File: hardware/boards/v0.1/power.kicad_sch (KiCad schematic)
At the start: 31 parts, among them IC3 SP3401-02UTG, J2 USB, U20 TPS62A02DRL, U23 BQ21040DBV, U31 FUSB302B01MPX, U32 LTC2942

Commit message: feat: route audio components
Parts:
- C17, C18, R29: footprint Capacitor_SMD:C_0402_1005Metric -> Capacitor_SMD:C_0603_1608Metric
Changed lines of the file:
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@@
 			)
 		)
-		(property "Footprint" "Capacitor_SMD:C_0402_1005Metric"
+		(property "Footprint" "Capacitor_SMD:C_0603_1608Metric"
 			(at 104.14 30.48 0)
 			(effects
@@
 			)
 		)
-		(property "Footprint" "Capacitor_SMD:C_0402_1005Metric"
+		(property "Footprint" "Capacitor_SMD:C_0603_1608Metric"
 			(at 127.508 46.99 90)
 			(effects
@@
 			)
 		)
-		(property "Footprint" "Capacitor_SMD:C_0402_1005Metric"
+		(property "Footprint" "Capacitor_SMD:C_0603_1608Metric"
 			(at 96.52 30.48 0)
 			(effects

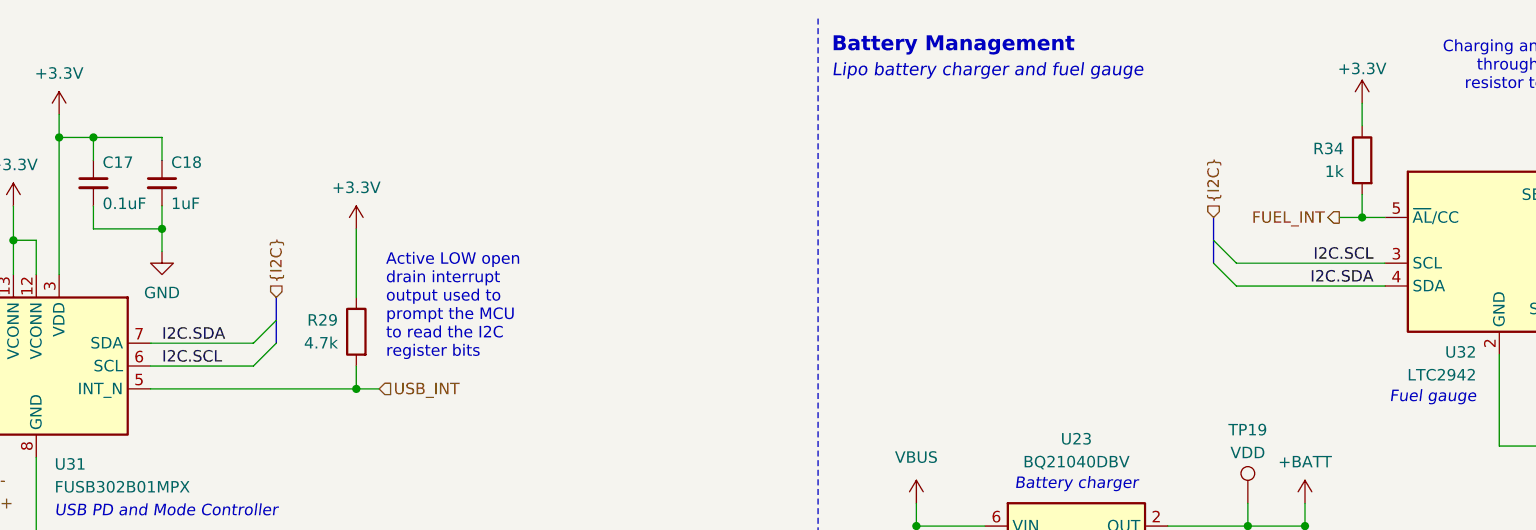
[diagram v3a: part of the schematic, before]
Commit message: feat: route dedicated audio I2C bus
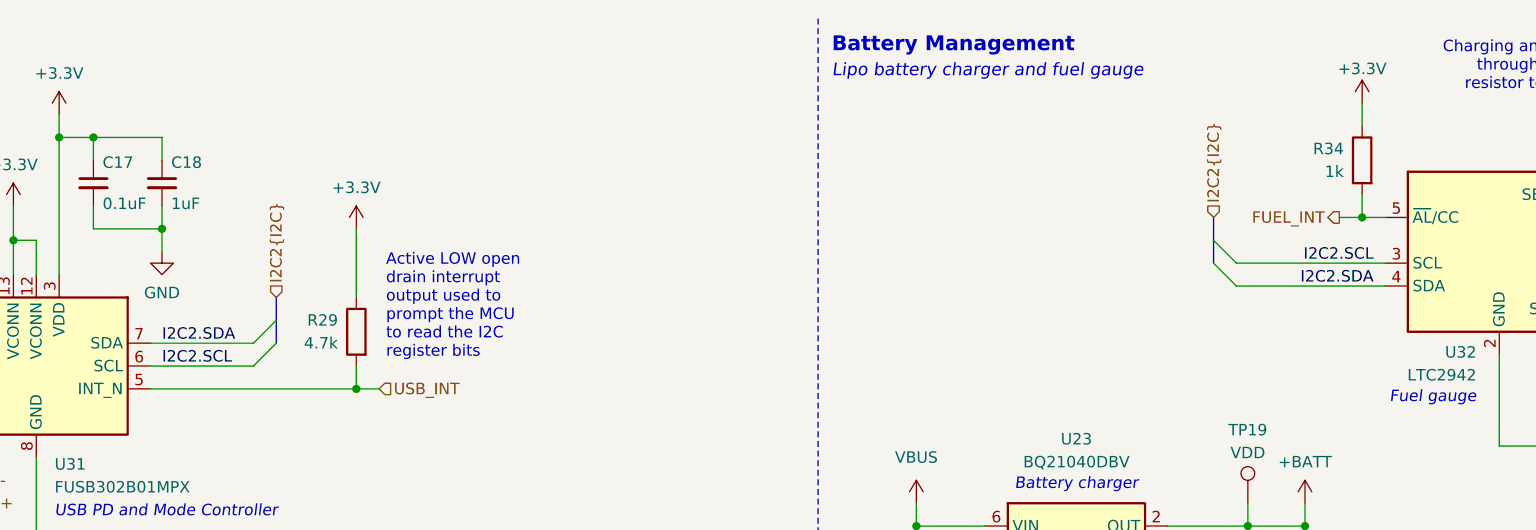
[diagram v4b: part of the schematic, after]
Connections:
- net I2C.SCL renamed I2C2.SCL
- net I2C.SDA renamed I2C2.SDA
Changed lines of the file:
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@@
 		)
 	)
-	(label "I2C.SCL"
+	(label "I2C2.SCL"
 		(at 238.76 39.37 180)
 		(effects
@@
 		)
 	)
-	(label "I2C.SDA"
+	(label "I2C2.SDA"
 		(at 104.14 48.26 0)
 		(effects
@@
 		)
 	)
-	(label "I2C.SDA"
+	(label "I2C2.SDA"
 		(at 238.76 41.91 180)
 		(effects
@@
 		)
 	)
-	(label "I2C.SCL"
+	(label "I2C2.SCL"
 		(at 104.14 50.8 0)
 		(effects
@@
 		)
 	)
-	(hierarchical_label "{I2C}"
+	(hierarchical_label "I2C2{I2C}"
 		(shape input)
 		(at 116.84 43.18 90)
@@
 		)
 	)
-	(hierarchical_label "{I2C}"
+	(hierarchical_label "I2C2{I2C}"
 		(shape input)
 		(at 220.98 34.29 90)

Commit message: feat: power system routing
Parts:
- added TP20: GND, TestPoint:TestPoint_Pad_D1.0mm, symbol Connector:TestPoint
- C12, C13, C9: footprint Capacitor_SMD:C_0805_2012Metric -> Capacitor_SMD:C_0603_1608Metric
- R2, R63, R72: footprint Capacitor_SMD:C_0402_1005Metric -> Resistor_SMD:R_0603_1608Metric
- R29: footprint Capacitor_SMD:C_0603_1608Metric -> Resistor_SMD:R_0603_1608Metric
- R33: value 100m -> 12m; footprint Capacitor_SMD:C_0402_1005Metric -> Resistor_SMD:R_2512_6332Metric_Pad1.40x3.35mm_HandSolder
- R34, R38: footprint Resistor_SMD:R_0402_1005Metric -> Resistor_SMD:R_0603_1608Metric
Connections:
- net GND: now also TP20.1
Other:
- note added: "I2C Address 1100100"
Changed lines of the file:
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@@
 		)
 	)
+	(text "I2C Address\n1100100"
+		(exclude_from_sim no)
+		(at 239.776 45.974 0)
+		(effects
+			(font
+				(size 1.27 1.27)
+				(color 132 132 132 1)
+			)
+			(justify right)
+		)
+	)
 	(text "Used by the STM32 to detect when a USB\ncable has been plugged in or removed.\n\nExpected signal < 4v"
 		(exclude_from_sim no)
@@
 	)
 	(junction
+		(at 212.09 86.36)
+		(diameter 0)
+		(color 0 0 0 0)
+	)
+	(junction
 		(at 67.31 153.67)
 		(diameter 0)
@@
 	(wire
 		(pts
-			(xy 205.74 86.36) (xy 223.52 86.36)
+			(xy 205.74 86.36) (xy 212.09 86.36)
 		)
 		(stroke
@@
 	(wire
 		(pts
+			(xy 212.09 86.36) (xy 223.52 86.36)
+		)
+		(stroke
+			(width 0)
+			(type default)
+		)
+	)
+	(wire
+		(pts
 			(xy 49.53 156.21) (xy 44.45 156.21)
 		)
@@
 	(wire
 		(pts
+			(xy 212.09 86.36) (xy 212.09 88.9)
+		)
+		(stroke
+			(width 0)
+			(type default)
+		)
+	)
+	(wire
+		(pts
 			(xy 72.39 185.42) (xy 72.39 186.69)
 		)
@@
 			)
 		)
-		(property "Value" "100m"
+		(property "Value" "12m"
 			(at 272.288 39.37 0)
 			(effects
@@
 			)
 		)
-		(property "Footprint" "Capacitor_SMD:C_0402_1005Metric"
+		(property "Footprint" "Resistor_SMD:R_2512_6332Metric_Pad1.40x3.35mm_HandSolder"
 			(at 276.098 38.1 90)
 			(effects
@@
 	)
 	(symbol
+		(lib_id "Connector:TestPoint")
+		(at 212.09 88.9 180)
+		(unit 1)
+		(exclude_from_sim no)
+		(in_bom yes)
+		(on_board yes)
+		(dnp no)
+		(property "Reference" "TP20"
+			(at 212.09 97.028 0)
+			(effects
+				(font
+					(size 1.27 1.27)
+				)
+			)
+		)
+		(property "Value" "GND"
+			(at 212.09 94.488 0)
+			(effects
+				(font
+					(size 1.27 1.27)
+				)
+			)
+		)
+		(property "Footprint" "TestPoint:TestPoint_Pad_D1.0mm"
+			(at 207.01 88.9 0)
+			(effects
+				(font
+					(size 1.27 1.27)
+				)
+				(hide yes)
+			)
+		)
+		(property "Datasheet" "~"
+			(at 207.01 88.9 0)
+			(effects
+				(font
+					(size 1.27 1.27)
+				)
+				(hide yes)
+			)
+		)
+		(property "Description" "test point"
+			(at 212.09 88.9 0)
+			(effects
+				(font
+					(size 1.27 1.27)
+				)
+				(hide yes)
+			)
+		)
+		(property "Arrow Part Number" ""
+			(at 212.09 88.9 0)
+			(effects
+				(font
+					(size 1.27 1.27)
+				)
+			)
+		)
+		(property "Arrow Price/Stock" ""
+			(at 212.09 88.9 0)
+			(effects
+				(font
+					(size 1.27 1.27)
+				)
+			)
+		)
+		(property "MANUFACTURER" ""
+			(at 212.09 88.9 0)
+			(effects
+				(font
+					(size 1.27 1.27)
+				)
+			)
+		)
+		(property "MAXIMUM_PACKAGE_HEIGHT" ""
+			(at 212.09 88.9 0)
+			(effects
+				(font
+					(size 1.27 1.27)
+				)
+			)
+		)
+		(property "PARTREV" ""
+			(at 212.09 88.9 0)
+			(effects
+				(font
+					(size 1.27 1.27)
+				)
+			)
+		)
+		(property "STANDARD" ""
+			(at 212.09 88.9 0)
+			(effects
+				(font
+					(size 1.27 1.27)
+				)
+			)
+		)
+		(property "Connector" ""
+			(at 212.09 88.9 0)
+			(effects
+				(font
+					(size 1.27 1.27)
+				)
+			)
+		)
+		(pin "1"
+		)
+		(instances
+			(project "pocket_synth"
+				(path "/485383b8-00f4-4405-b270-de249939cff4/4ddef61a-efa7-4012-86d6-37c4f1088d14"
+					(reference "TP20")
+					(unit 1)
+				)
+			)
+		)
+	)
+	(symbol
 		(lib_id "power:GND")
 		(at 205.74 88.9 0)
@@
 			)
 		)
-		(property "Footprint" "Resistor_SMD:R_0402_1005Metric"
+		(property "Footprint" "Resistor_SMD:R_0603_1608Metric"
 			(at 239.268 27.94 90)
 			(effects
@@
 			)
 		)
-		(property "Footprint" "Capacitor_SMD:C_0805_2012Metric"
+		(property "Footprint" "Capacitor_SMD:C_0603_1608Metric"
 			(at 75.2348 163.83 0)
 			(effects
@@
 			)
 		)
-		(property "Footprint" "Resistor_SMD:R_0402_1005Metric"
+		(property "Footprint" "Resistor_SMD:R_0603_1608Metric"
 			(at 191.262 80.01 90)
 			(effects
@@
 			)
 		)
-		(property "Footprint" "Capacitor_SMD:C_0402_1005Metric"
+		(property "Footprint" "Resistor_SMD:R_0603_1608Metric"
 			(at 72.39 189.23 0)
 			(effects
@@
 			)
 		)
-		(property "Footprint" "Capacitor_SMD:C_0805_2012Metric"
+		(property "Footprint" "Capacitor_SMD:C_0603_1608Metric"
 			(at 17.4752 175.26 0)
 			(effects
@@
 			)
 		)
-		(property "Footprint" "Capacitor_SMD:C_0402_1005Metric"
+		(property "Footprint" "Resistor_SMD:R_0603_1608Metric"
 			(at 91.948 179.07 90)
 			(effects
@@
 			)
 		)
-		(property "Footprint" "Capacitor_SMD:C_0603_1608Metric"
+		(property "Footprint" "Resistor_SMD:R_0603_1608Metric"
 			(at 127.508 46.99 90)
 			(effects
@@
 			)
 		)
-		(property "Footprint" "Capacitor_SMD:C_0805_2012Metric"
+		(property "Footprint" "Capacitor_SMD:C_0603_1608Metric"
 			(at 66.3448 163.83 0)
 			(effects
@@
 			)
 		)
-		(property "Footprint" "Capacitor_SMD:C_0402_1005Metric"
+		(property "Footprint" "Resistor_SMD:R_0603_1608Metric"
 			(at 77.47 194.31 0)
 			(effects

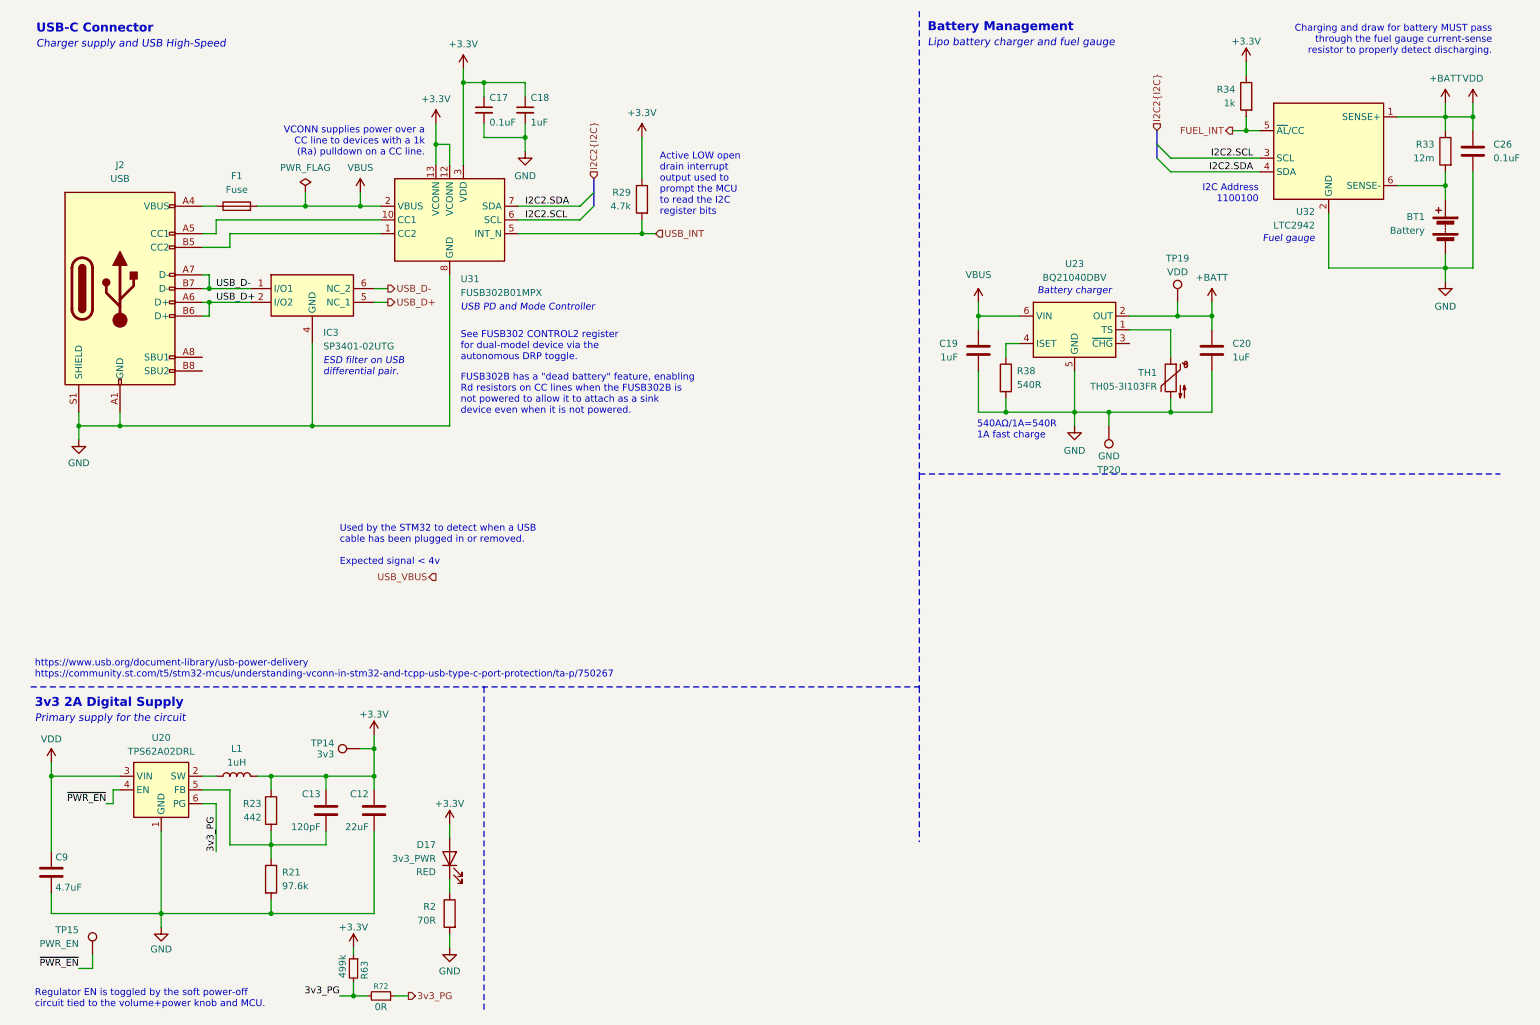
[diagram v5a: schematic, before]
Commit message: feat: add missing power button controller
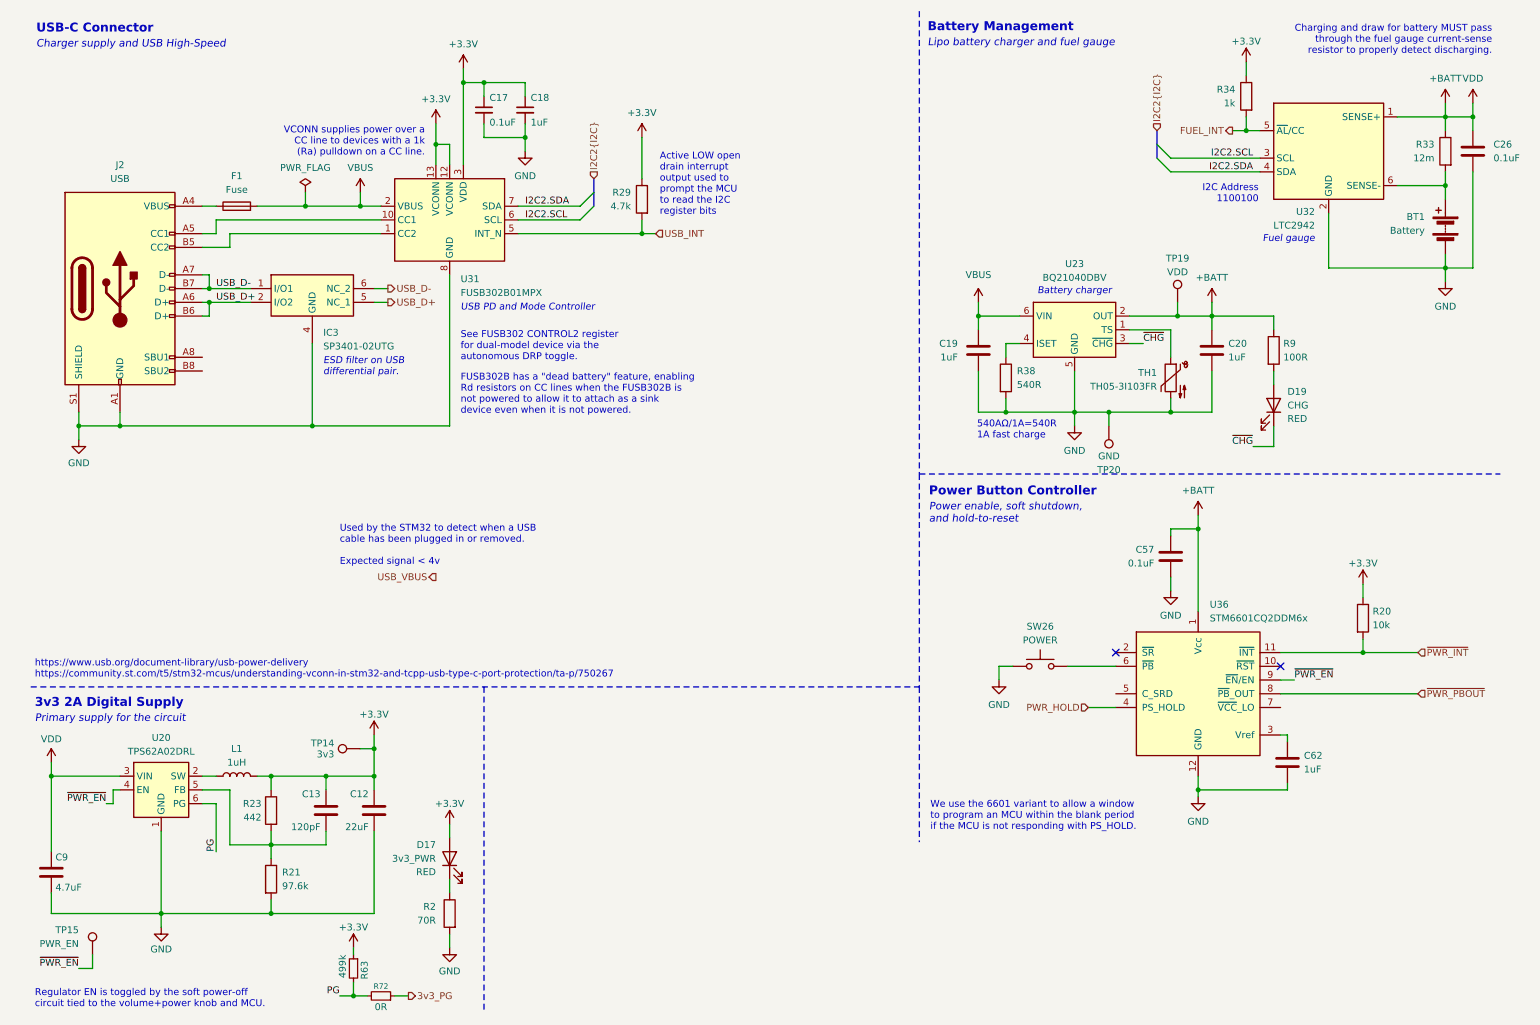
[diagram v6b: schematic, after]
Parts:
- added C57: 0.1uF, Capacitor_SMD:C_0402_1005Metric, symbol Device:C
- added C62: 1uF, Capacitor_SMD:C_0402_1005Metric, symbol Device:C
- added D19: CHG, LED_SMD:LED_0805_2012Metric_Pad1.15x1.40mm_HandSolder, symbol Device:LED
- added R20: 10k, Resistor_SMD:R_0402_1005Metric, symbol Device:R
- added R9: 100R, Resistor_SMD:R_0603_1608Metric, symbol Device:R
- added SW26: POWER, Button_Switch_SMD:SW_SPST_B3U-1000P, symbol Switch:SW_Push
- added U36: STM6601CQ2DDM6x, Package_DFN_QFN:TDFN-12_2x3mm_P0.5mm, symbol Power_Management:STM6601
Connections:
- net +3.3V: now also R20.1
- net +BATT: now also C57.1, R9.1, U36.1 (Vcc)
- net 3v3_PG: no longer R63.2, R72.2, U20.6 (PG)
- net GND: now also C57.2, C62.2, SW26.1, U36.12 (GND)
- net ~{PWR_EN}: now also U36.9 (~{EN}/EN)
- net ~{CHG}: now reaches U23.3 (~{CHG})
- net ~{CHG}: now also D19.1 (K)
- new net: SW26.2, U36.6 (~{PB})
- new net: C62.1, U36.3 (Vref)
- new net: D19.2 (A), R9.2
- new net PG: R63.2, R72.2, U20.6 (PG)
- new net PWR_HOLD: U36.4 (PS_HOLD)
- new net ~{PWR_INT}: R20.2, U36.11 (~{INT})
- new net ~{PWR_PBOUT}: U36.8 (~{PB}_OUT)
- no-connect marks 0 -> 2
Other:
- note added: "Power Button Controller"
- note added: "Power enable, soft shutdown, and hold-to-reset"
- note added: "We use the 6601 variant to allow a window to program an MCU within the blank period if the MCU is not responding with PS_HOLD."

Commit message: feat: add test points and top and bottom ground pours
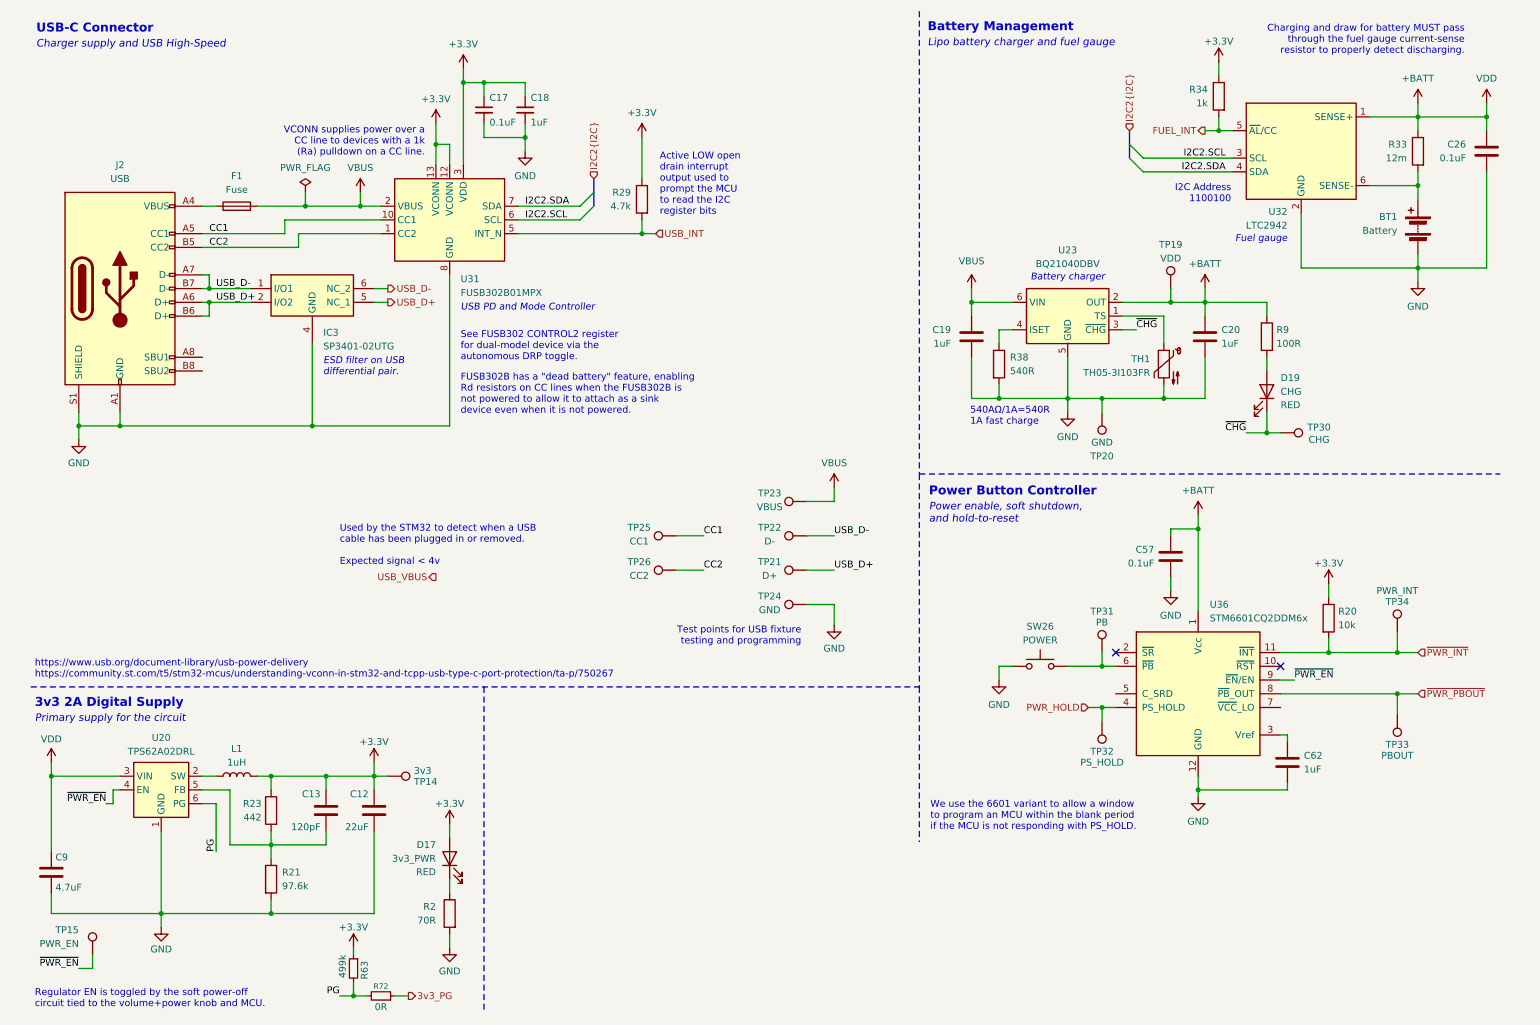
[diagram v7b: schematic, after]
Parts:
- added TP21: D+, TestPoint:TestPoint_Pad_D1.0mm, symbol Connector:TestPoint
- added TP22: D-, TestPoint:TestPoint_Pad_D1.0mm, symbol Connector:TestPoint
- added TP23: VBUS, TestPoint:TestPoint_Pad_D1.0mm, symbol Connector:TestPoint
- added TP24: GND, TestPoint:TestPoint_Pad_D1.0mm, symbol Connector:TestPoint
- added TP25: CC1, TestPoint:TestPoint_Pad_D1.0mm, symbol Connector:TestPoint
- added TP26: CC2, TestPoint:TestPoint_Pad_D1.0mm, symbol Connector:TestPoint
- added TP30: CHG, TestPoint:TestPoint_Pad_D1.0mm, symbol Connector:TestPoint
- added TP31: PB, TestPoint:TestPoint_Pad_D1.0mm, symbol Connector:TestPoint
- added TP32: PS_HOLD, TestPoint:TestPoint_Pad_D1.0mm, symbol Connector:TestPoint
- added TP33: PBOUT, TestPoint:TestPoint_Pad_D1.0mm, symbol Connector:TestPoint
- added TP34: PWR_INT, TestPoint:TestPoint_Pad_D1.0mm, symbol Connector:TestPoint
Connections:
- net GND: now also TP24.1
- net PWR_HOLD: now also TP32.1
- net USB_D+: now also TP21.1
- net USB_D-: now also TP22.1
- net VBUS: now also TP23.1
- net ~{CHG}: now also TP30.1
- net ~{PWR_INT}: now also TP34.1
- net ~{PWR_PBOUT}: now also TP33.1
- net at SW26.2, U36.6 (~{PB}): now also TP31.1
- net CC2: now reaches J2.B5 (CC2), U31.1 (CC2), U31.14 (CC2)
- net CC2: now also TP26.1
- net CC1: now reaches J2.A5 (CC1), U31.10 (CC1), U31.11 (CC1)
- net CC1: now also TP25.1
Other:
- note added: "Test points for USB fixture testing and programming"
- moved on the sheet: BT1, C19, C20, C26, D19, R20, R33, R34, R38, R9, TH1, TP14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
